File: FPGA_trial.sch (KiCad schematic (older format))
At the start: 5 parts

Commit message: FPGA symbol edited for second time
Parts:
- removed U? (x5): GW1N-9LQ100_Edited, symbol OpenVent:GW1N-9LQ100_Edited
- added U? (x5): GW1N-9LQ100_Edited_2, symbol OpenVent:GW1N-9LQ100_Edited_2
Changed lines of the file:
@@
 Trial sheet to test updated FPGA symbol, will be removed once FPGA symbol agreed upon. Note that the asterisks still need to be double checked. LM 10/03/21
 $Comp
-L OpenVent:GW1N-9LQ100_Edited U?
-U 1 1 604C9D4E
-P 1050 2750
-F 0 "U?" H 1775 4165 50  0000 C CNN
-F 1 "GW1N-9LQ100_Edited" H 1775 4074 50  0000 C CNN
-F 2 "" H 350 4400 50  0001 C CNN
-F 3 "" H 350 4400 50  0001 C CNN
-	1    1050 2750
+L OpenVent:GW1N-9LQ100_Edited_2 U?
+U 1 1 604F0EDE
+P 3000 1500
+F 0 "U?" H 3025 1665 50  0000 C CNN
+F 1 "GW1N-9LQ100_Edited_2" H 3025 1574 50  0000 C CNN
+F 2 "" H 6300 600 50  0001 C CNN
+F 3 "" H 6300 600 50  0001 C CNN
+	1    3000 1500
 	1    0    0    -1
 $EndComp
 $Comp
-L OpenVent:GW1N-9LQ100_Edited U?
-U 2 1 604CB5AC
-P 3900 1500
-F 0 "U?" H 3900 1748 50  0000 C CNN
-F 1 "GW1N-9LQ100_Edited" H 3900 1657 50  0000 C CNN
-F 2 "" H 3200 3150 50  0001 C CNN
-F 3 "" H 3200 3150 50  0001 C CNN
-	2    3900 1500
+L OpenVent:GW1N-9LQ100_Edited_2 U?
+U 2 1 604F14AE
+P 2950 3350
+F 0 "U?" H 2975 3598 50  0000 C CNN
+F 1 "GW1N-9LQ100_Edited_2" H 2975 3507 50  0000 C CNN
+F 2 "" H 6250 2450 50  0001 C CNN
+F 3 "" H 6250 2450 50  0001 C CNN
+	2    2950 3350
 	1    0    0    -1
 $EndComp
 $Comp
-L OpenVent:GW1N-9LQ100_Edited U?
-U 3 1 604CD2F6
-P 5900 1500
-F 0 "U?" H 5875 1748 50  0000 C CNN
-F 1 "GW1N-9LQ100_Edited" H 5875 1657 50  0000 C CNN
-F 2 "" H 5200 3150 50  0001 C CNN
-F 3 "" H 5200 3150 50  0001 C CNN
-	3    5900 1500
+L OpenVent:GW1N-9LQ100_Edited_2 U?
+U 4 1 604F1FF3
+P 3000 4500
+F 0 "U?" H 2975 4748 50  0000 C CNN
+F 1 "GW1N-9LQ100_Edited_2" H 2975 4657 50  0000 C CNN
+F 2 "" H 6300 3600 50  0001 C CNN
+F 3 "" H 6300 3600 50  0001 C CNN
+	4    3000 4500
 	1    0    0    -1
 $EndComp
 $Comp
-L OpenVent:GW1N-9LQ100_Edited U?
-U 4 1 604CE582
-P 2200 4150
-F 0 "U?" H 2175 4398 50  0000 C CNN
-F 1 "GW1N-9LQ100_Edited" H 2175 4307 50  0000 C CNN
-F 2 "" H 1500 5800 50  0001 C CNN
-F 3 "" H 1500 5800 50  0001 C CNN
-	4    2200 4150
+L OpenVent:GW1N-9LQ100_Edited_2 U?
+U 5 1 604F2C0B
+P 6100 3850
+F 0 "U?" H 6058 4098 50  0000 C CNN
+F 1 "GW1N-9LQ100_Edited_2" H 6058 4007 50  0000 C CNN
+F 2 "" H 9400 2950 50  0001 C CNN
+F 3 "" H 9400 2950 50  0001 C CNN
+	5    6100 3850
 	1    0    0    -1
 $EndComp
 $Comp
-L OpenVent:GW1N-9LQ100_Edited U?
-U 5 1 604D09E3
-P 5500 4150
-F 0 "U?" H 5525 4398 50  0000 C CNN
-F 1 "GW1N-9LQ100_Edited" H 5525 4307 50  0000 C CNN
-F 2 "" H 4800 5800 50  0001 C CNN
-F 3 "" H 4800 5800 50  0001 C CNN
-	5    5500 4150
+L OpenVent:GW1N-9LQ100_Edited_2 U?
+U 6 1 604F3921
+P 6050 1700
+F 0 "U?" H 6075 1948 50  0000 C CNN
+F 1 "GW1N-9LQ100_Edited_2" H 6075 1857 50  0000 C CNN
+F 2 "" H 9350 800 50  0001 C CNN
+F 3 "" H 9350 800 50  0001 C CNN
+	6    6050 1700
 	1    0    0    -1
 $EndComp

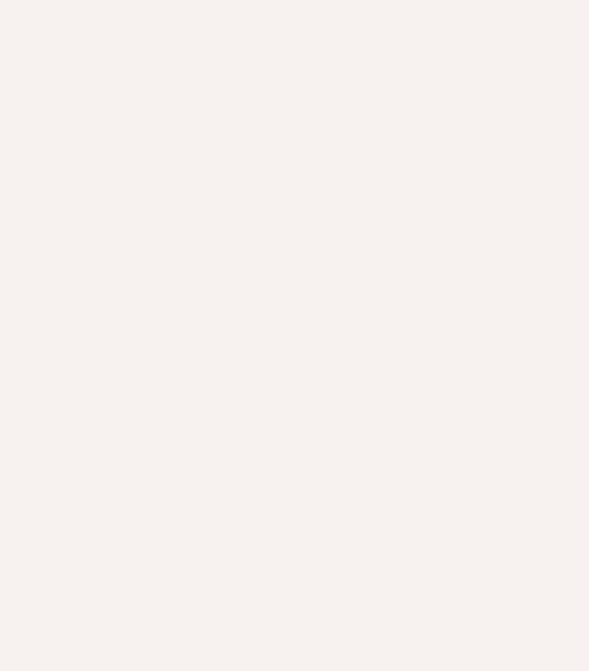
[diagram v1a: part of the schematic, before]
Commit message: Update FPGA symbol, remove FPGA_trial sheet
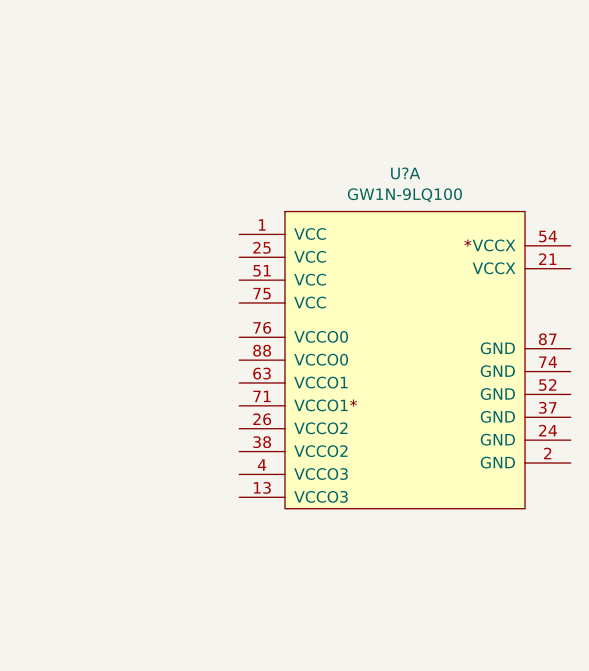
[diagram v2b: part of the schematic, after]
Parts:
- added U?: GW1N-9LQ100, symbol OpenVent:GW1N-9LQ100
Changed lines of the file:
@@
+	1    0    0    -1
+$EndComp
+$Comp
+L OpenVent:GW1N-9LQ100 U?
+U 1 1 60534135
+P 9200 1650
+F 0 "U?" H 9225 1815 50  0000 C CNN
+F 1 "GW1N-9LQ100" H 9225 1724 50  0000 C CNN
+F 2 "" H 12500 750 50  0001 C CNN
+F 3 "" H 12500 750 50  0001 C CNN
+	1    9200 1650
 	1    0    0    -1
 $EndComp
